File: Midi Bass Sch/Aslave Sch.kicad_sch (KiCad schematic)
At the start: 12 parts, among them J8 A SLAVE ISCP, SW4 A-slave Reset, U8 PIC16F1789

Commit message: finished troubleshooting section
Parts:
- renumbered J8 to J10
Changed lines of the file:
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@@
 		(dnp no)
 		(fields_autoplaced yes)
-		(property "Reference" "#PWR079"
+		(property "Reference" "#PWR081"
 			(at 36.83 135.89 0)
 			(effects
@@
 			(project "Midi Bass Sch"
 				(path "/06818073-fb22-48ee-acc5-6dedd827034e/c3b9cd48-3fcf-4fda-9d60-ef0911073906"
-					(reference "#PWR079")
+					(reference "#PWR081")
 					(unit 1)
 				)
@@
 		(dnp no)
 		(fields_autoplaced yes)
-		(property "Reference" "#PWR082"
+		(property "Reference" "#PWR084"
 			(at 63.1444 113.1316 0)
 			(effects
@@
 			(project "Midi Bass Sch"
 				(path "/06818073-fb22-48ee-acc5-6dedd827034e/c3b9cd48-3fcf-4fda-9d60-ef0911073906"
-					(reference "#PWR082")
+					(reference "#PWR084")
 					(unit 1)
 				)
@@
 		(dnp no)
 		(fields_autoplaced yes)
-		(property "Reference" "#PWR087"
+		(property "Reference" "#PWR089"
 			(at 200.66 119.38 0)
 			(effects
@@
 			(project "Midi Bass Sch"
 				(path "/06818073-fb22-48ee-acc5-6dedd827034e/c3b9cd48-3fcf-4fda-9d60-ef0911073906"
-					(reference "#PWR087")
+					(reference "#PWR089")
 					(unit 1)
 				)
@@
 		(dnp no)
 		(fields_autoplaced yes)
-		(property "Reference" "#PWR084"
+		(property "Reference" "#PWR086"
 			(at 113.03 153.67 0)
 			(effects
@@
 			(project "Midi Bass Sch"
 				(path "/06818073-fb22-48ee-acc5-6dedd827034e/c3b9cd48-3fcf-4fda-9d60-ef0911073906"
-					(reference "#PWR084")
+					(reference "#PWR086")
 					(unit 1)
 				)
@@
 		(dnp no)
 		(fields_autoplaced yes)
-		(property "Reference" "#PWR080"
+		(property "Reference" "#PWR082"
 			(at 46.6344 50.9016 0)
 			(effects
@@
 			(project "Midi Bass Sch"
 				(path "/06818073-fb22-48ee-acc5-6dedd827034e/c3b9cd48-3fcf-4fda-9d60-ef0911073906"
-					(reference "#PWR080")
+					(reference "#PWR082")
 					(unit 1)
 				)
@@
 		(dnp no)
 		(fields_autoplaced yes)
-		(property "Reference" "#PWR081"
+		(property "Reference" "#PWR083"
 			(at 41.91 63.5 0)
 			(effects
@@
 			(project "Midi Bass Sch"
 				(path "/06818073-fb22-48ee-acc5-6dedd827034e/c3b9cd48-3fcf-4fda-9d60-ef0911073906"
-					(reference "#PWR081")
+					(reference "#PWR083")
 					(unit 1)
 				)
@@
 		(dnp no)
 		(fields_autoplaced yes)
-		(property "Reference" "#PWR085"
+		(property "Reference" "#PWR087"
 			(at 120.2944 16.6116 0)
 			(effects
@@
 			(project "Midi Bass Sch"
 				(path "/06818073-fb22-48ee-acc5-6dedd827034e/c3b9cd48-3fcf-4fda-9d60-ef0911073906"
-					(reference "#PWR085")
+					(reference "#PWR087")
 					(unit 1)
 				)
@@
 		(dnp no)
 		(fields_autoplaced yes)
-		(property "Reference" "#PWR083"
+		(property "Reference" "#PWR085"
 			(at 58.42 134.62 0)
 			(effects
@@
 			(project "Midi Bass Sch"
 				(path "/06818073-fb22-48ee-acc5-6dedd827034e/c3b9cd48-3fcf-4fda-9d60-ef0911073906"
-					(reference "#PWR083")
+					(reference "#PWR085")
 					(unit 1)
 				)
@@
 		(dnp no)
 		(fields_autoplaced yes)
-		(property "Reference" "J8"
+		(property "Reference" "J10"
 			(at 30.48 50.8 0)
 			(effects
@@
 			(project "Midi Bass Sch"
 				(path "/06818073-fb22-48ee-acc5-6dedd827034e/c3b9cd48-3fcf-4fda-9d60-ef0911073906"
-					(reference "J8")
+					(reference "J10")
 					(unit 1)
 				)
@@
 		(dnp no)
 		(fields_autoplaced yes)
-		(property "Reference" "#PWR086"
+		(property "Reference" "#PWR088"
 			(at 186.69 121.92 0)
 			(effects
@@
 			(project "Midi Bass Sch"
 				(path "/06818073-fb22-48ee-acc5-6dedd827034e/c3b9cd48-3fcf-4fda-9d60-ef0911073906"
-					(reference "#PWR086")
-					(unit 1)
-				)
+					(reference "#PWR088")
+					(unit 1)
+				)

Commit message: began getting images for schematic appendix
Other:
- title: (none) -> A-Slave Processor Schematic
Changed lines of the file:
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@@
 	(generator_version "8.0")
 	(paper "A")
+	(title_block
+		(title "A-Slave Processor Schematic")
+		(date "2024-12-10")
+		(rev "A")
+	)
 	(junction
 		(at 58.42 128.27)

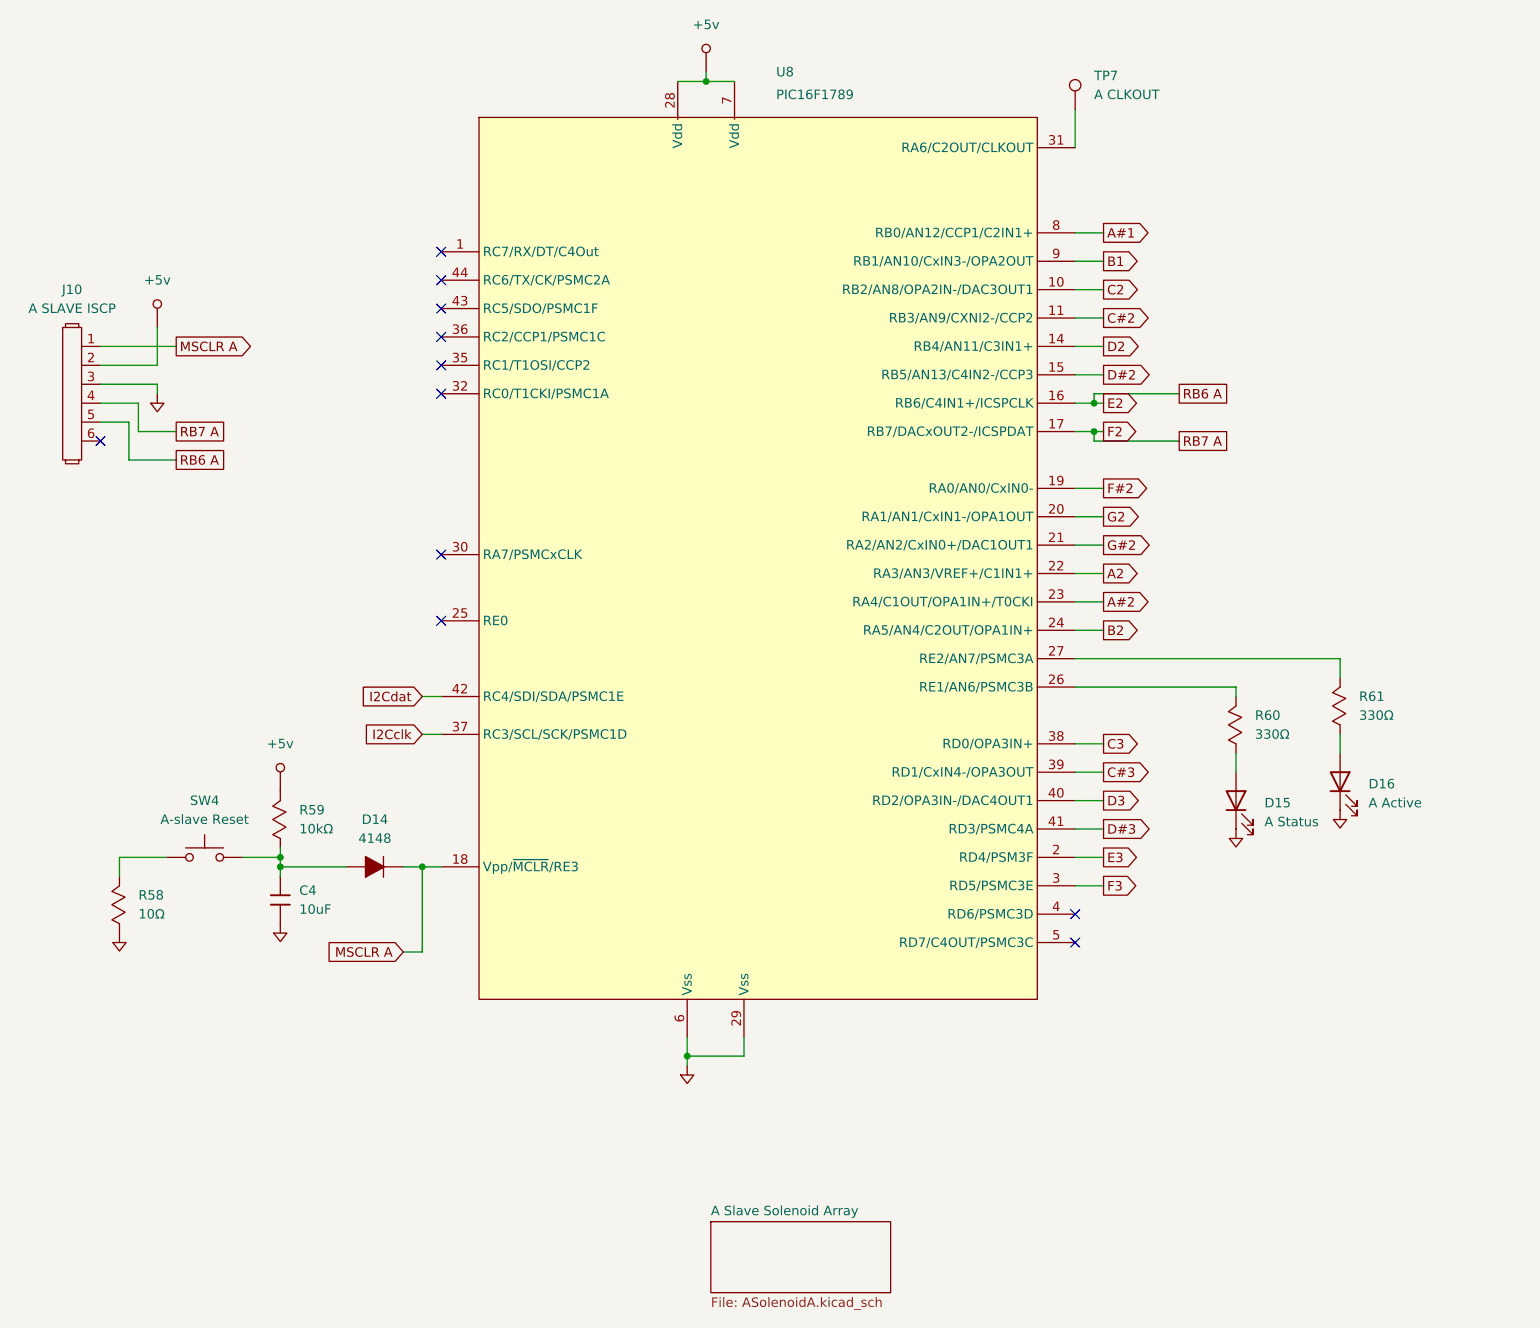
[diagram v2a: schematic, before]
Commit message: began working on pcb layout deleted extra schematics for solenoid break out board
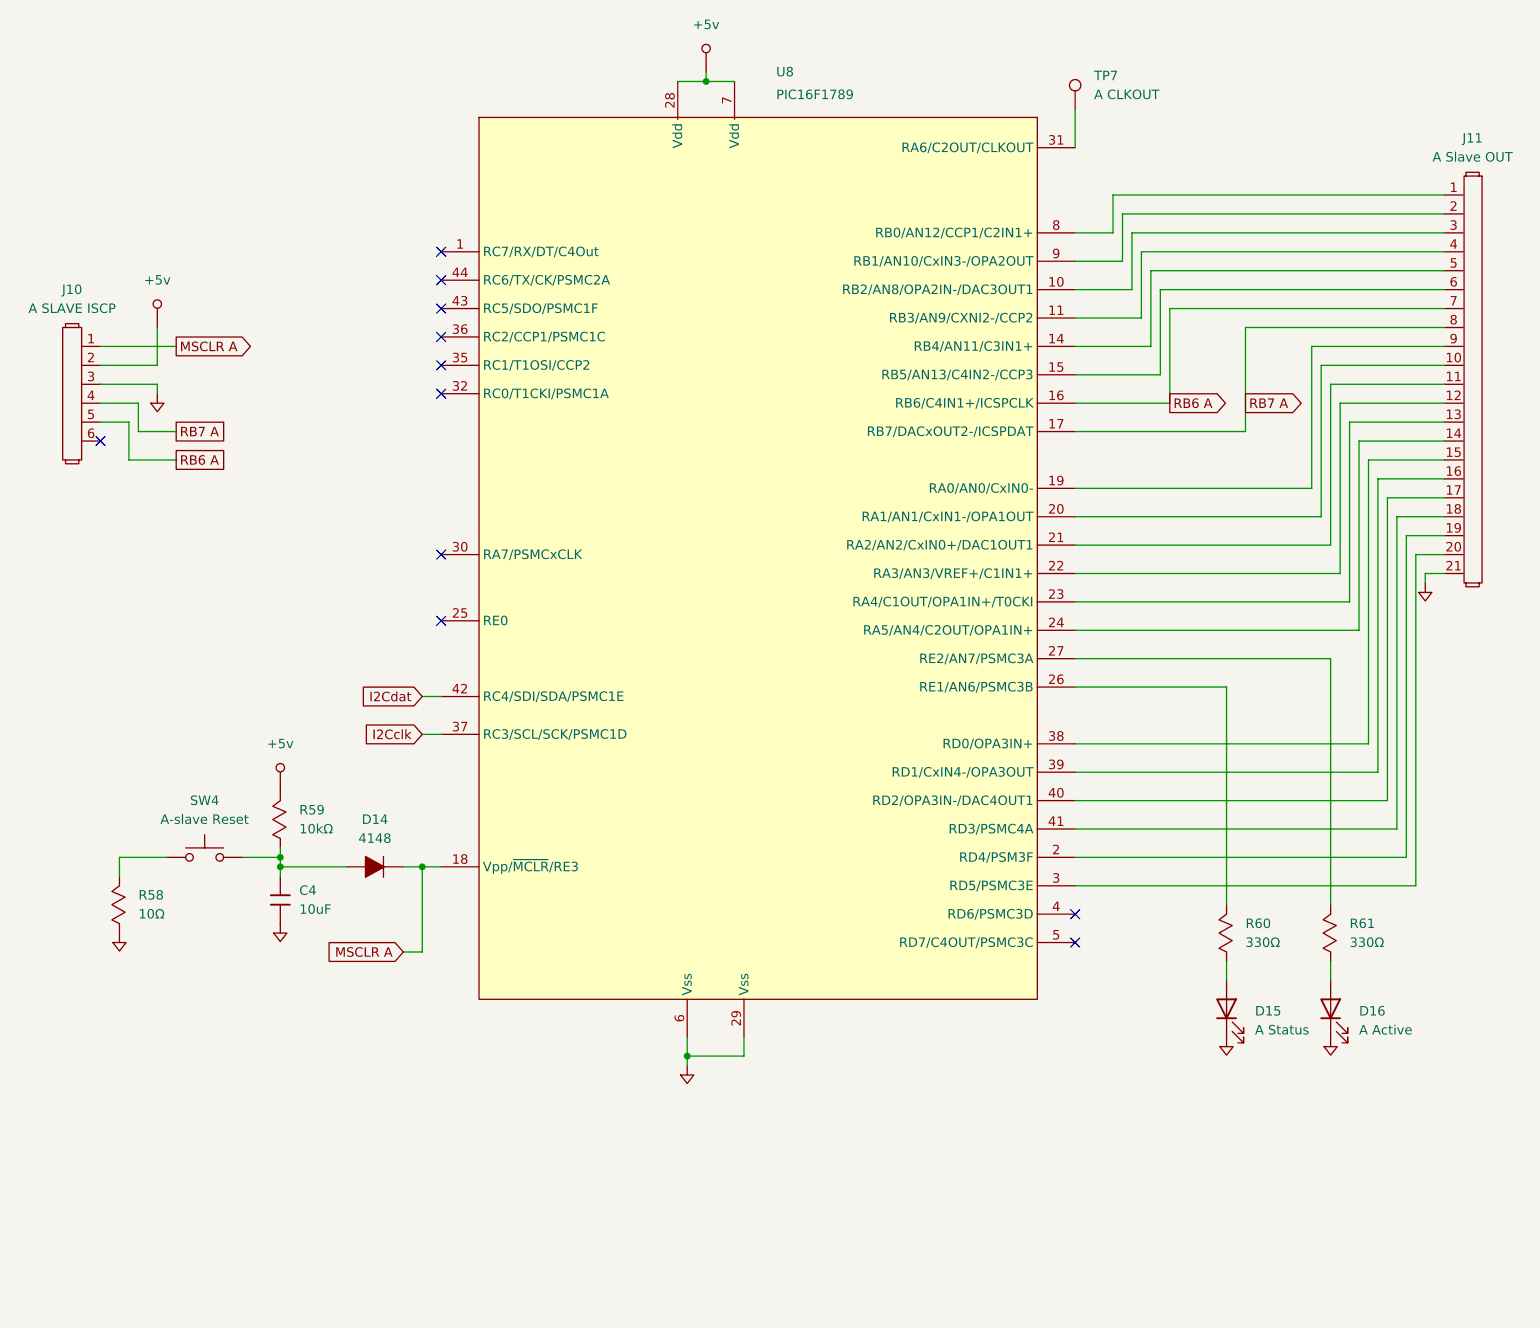
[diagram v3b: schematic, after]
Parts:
- added J11: A Slave OUT, Connector_PinHeader_2.54mm:PinHeader_1x21_P2.54mm_Vertical, symbol Owen's Symbols:Header_1x21
- SW4: footprint (none) -> Button_Switch_THT:SW_PUSH_6mm_H5mm
- TP7: footprint (none) -> Connector_PinHeader_2.54mm:PinHeader_1x01_P2.54mm_Vertical
- U8: footprint (none) -> OF footprints:TQFN-44_7x7_Pitch0.4mm
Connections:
- net GND: now also J11.21
- net A#1: no longer names the net of U8.8 (RB0/AN12/CCP1/C2IN1+)
- net A#1: now also J11.1
- net A#2: no longer names the net of U8.42 (RC4/SDI/SDA/PSMC1E)
- net A#2: now also J11.13
- net A2: no longer names the net of U8.37 (RC3/SCL/SCK/PSMC1D)
- net A2: now also J11.12
- net B1: no longer names the net of U8.9 (RB1/AN10/CxIN3-/OPA2OUT)
- net B1: now also J11.2
- net B2: no longer names the net of U8.43 (RC5/SDO/PSMC1F)
- net B2: now also J11.14
- net C#2: no longer names the net of U8.11 (RB3/AN9/CXNI2-/CCP2)
- net C#2: now also J11.4
- net C#3: no longer names the net of U8.39 (RD1/CxIN4-/OPA3OUT)
- net C#3: now also J11.16
- net C2: no longer names the net of U8.10 (RB2/AN8/OPA2IN-/DAC3OUT1)
- net C2: now also J11.3
- net C3: no longer names the net of U8.38 (RD0/OPA3IN+)
- net C3: now also J11.15
- net D#2: no longer names the net of U8.15 (RB5/AN13/C4IN2-/CCP3)
- net D#2: now also J11.6
- net D#3: no longer names the net of U8.41 (RD3/PSMC4A)
- net D#3: now also J11.18
- net D2: no longer names the net of U8.14 (RB4/AN11/C3IN1+)
- net D2: now also J11.5
- net D3: no longer names the net of U8.40 (RD2/OPA3IN-/DAC4OUT1)
- net D3: now also J11.17
- net E2 renamed RB6 A
- net RB6 A: now also J11.7
- net E3: no longer names the net of U8.2 (RD4/PSM3F)
- net E3: now also J11.19
- net F#2: no longer names the net of U8.32 (RC0/T1CKI/PSMC1A)
- net F#2: now also J11.9
- net F2 renamed RB7 A
- net RB7 A: now also J11.8
- net F3: no longer names the net of U8.3 (RD5/PSMC3E)
- net F3: now also J11.20
- net G#2: no longer names the net of U8.36 (RC2/CCP1/PSMC1C)
- net G#2: now also J11.11
- net G2: no longer names the net of U8.35 (RC1/T1OSI/CCP2)
- net G2: now also J11.10
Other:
- removed sheet A Slave Solenoid Array
- moved on the sheet: D15, D16, R60, R61

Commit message: updated motherboard pcb
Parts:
- J11: footprint Connector_PinHeader_2.54mm:PinHeader_1x21_P2.54mm_Vertical -> OF Footprints:PinHeader_2x21_P2.54mm_Vertical
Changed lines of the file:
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@@
 			)
 		)
-		(property "Footprint" "Connector_PinHeader_2.54mm:PinHeader_1x21_P2.54mm_Vertical"
+		(property "Footprint" "OF Footprints:PinHeader_2x21_P2.54mm_Vertical"
 			(at 218.44 34.29 0)
 			(effects
